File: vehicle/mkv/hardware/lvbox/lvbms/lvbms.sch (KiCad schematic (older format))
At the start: 135 parts, among them J1 CONN_02X03, J2 NanoFit_RA_SMT_04, J3 NanoFit_RA_SMT_02, J4 NanoFit_RA_SMT_02, J5 NanoFit_RA_SMT_02, J6 NanoFit_RA_SMT_02, J7 NanoFit_RA_SMT_02, J8 NanoFit_RA_SMT_06_A, J9 NanoFit_RA_SMT_02, Q1 NSS1C201MZ4, Q2 SQM110P06, Q3 SSM3K333R, Q4 SSM3K333R, Q5 SQM110P06, Q6 BSS138, Q7 SQM110P06, Q8 SQM110P06, U1 MCP2561-E_SN, U10 ACHS-7124, U11 redcube-7461057, U2 ATMEGA16M1, U3 LTC6810HG-2, U4 LT3066IMSE-5, U5 LT1017IS8, U9 redcube-7461057, Y1 Crystal_SMD

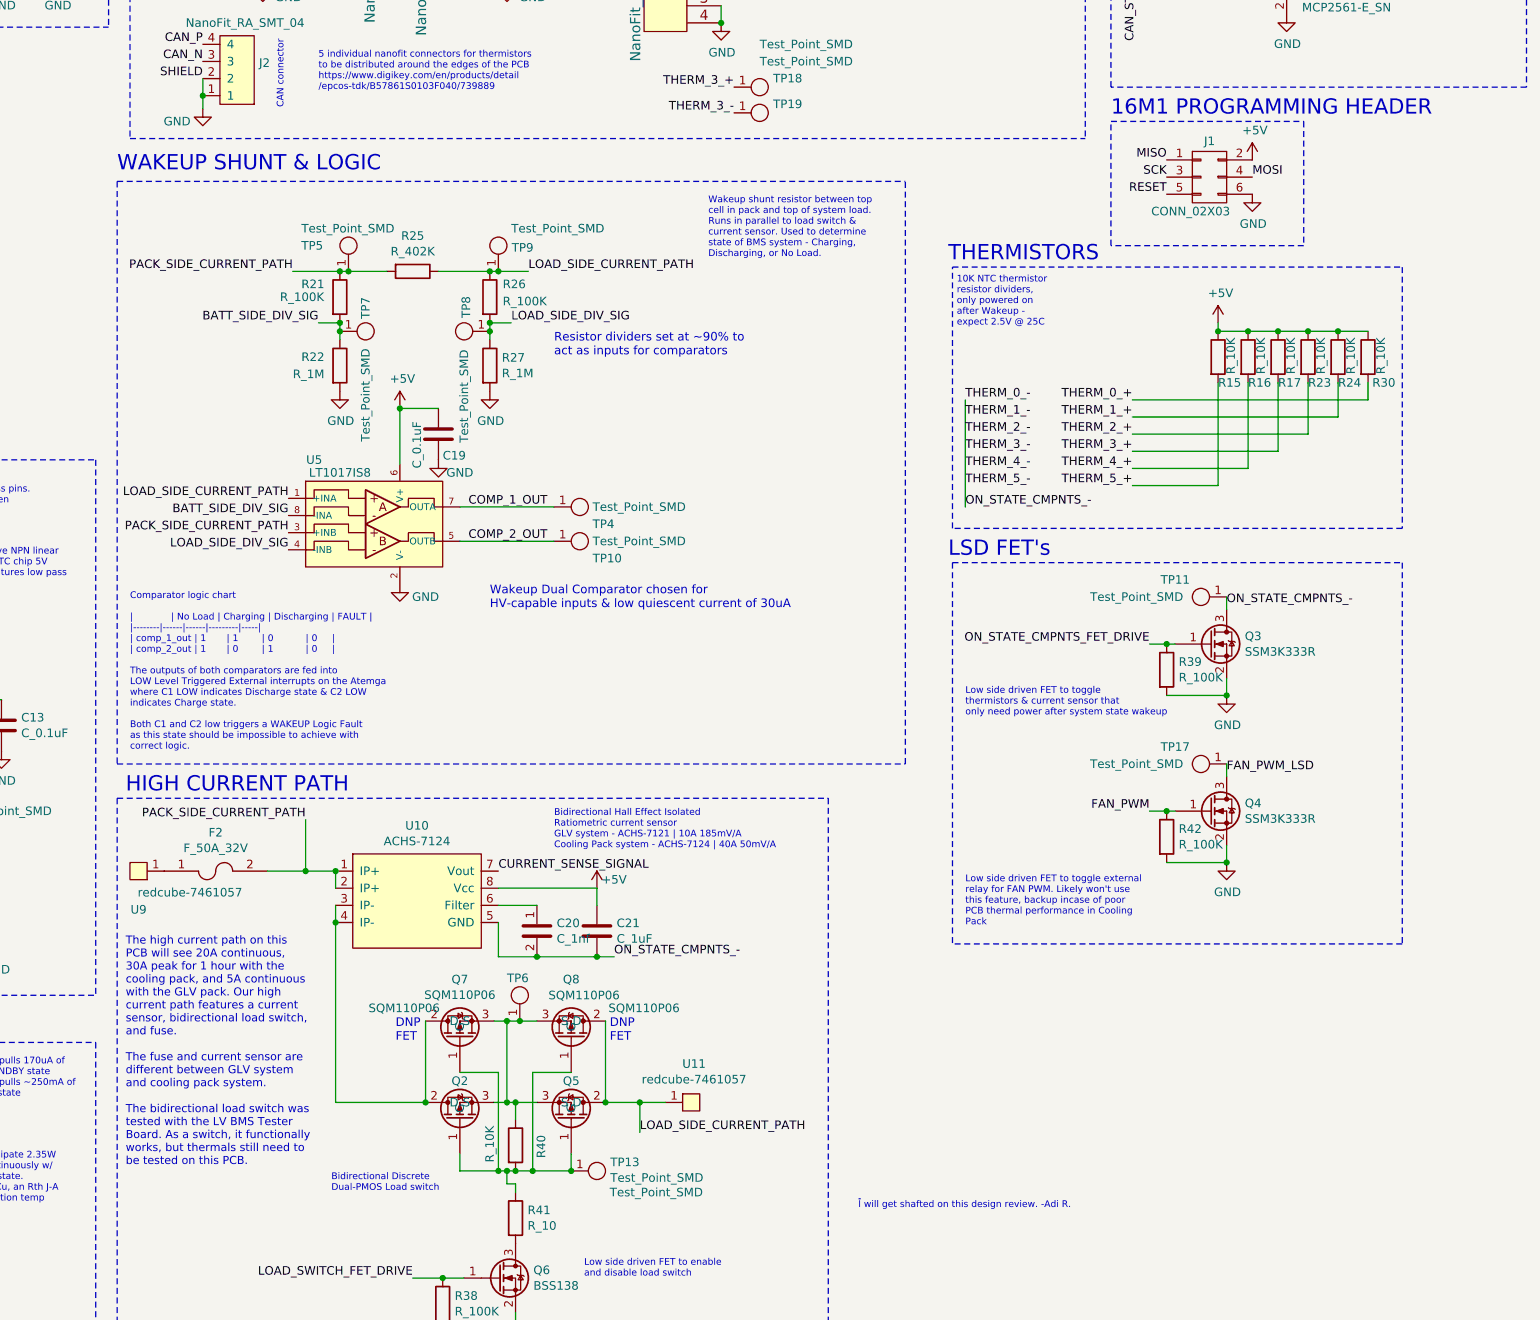
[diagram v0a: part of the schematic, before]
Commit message: updated SPI lib for peripheral A, testing LVBMS SPI, spi_write_read inside ltc681x.c read68 cmd blocks superloop
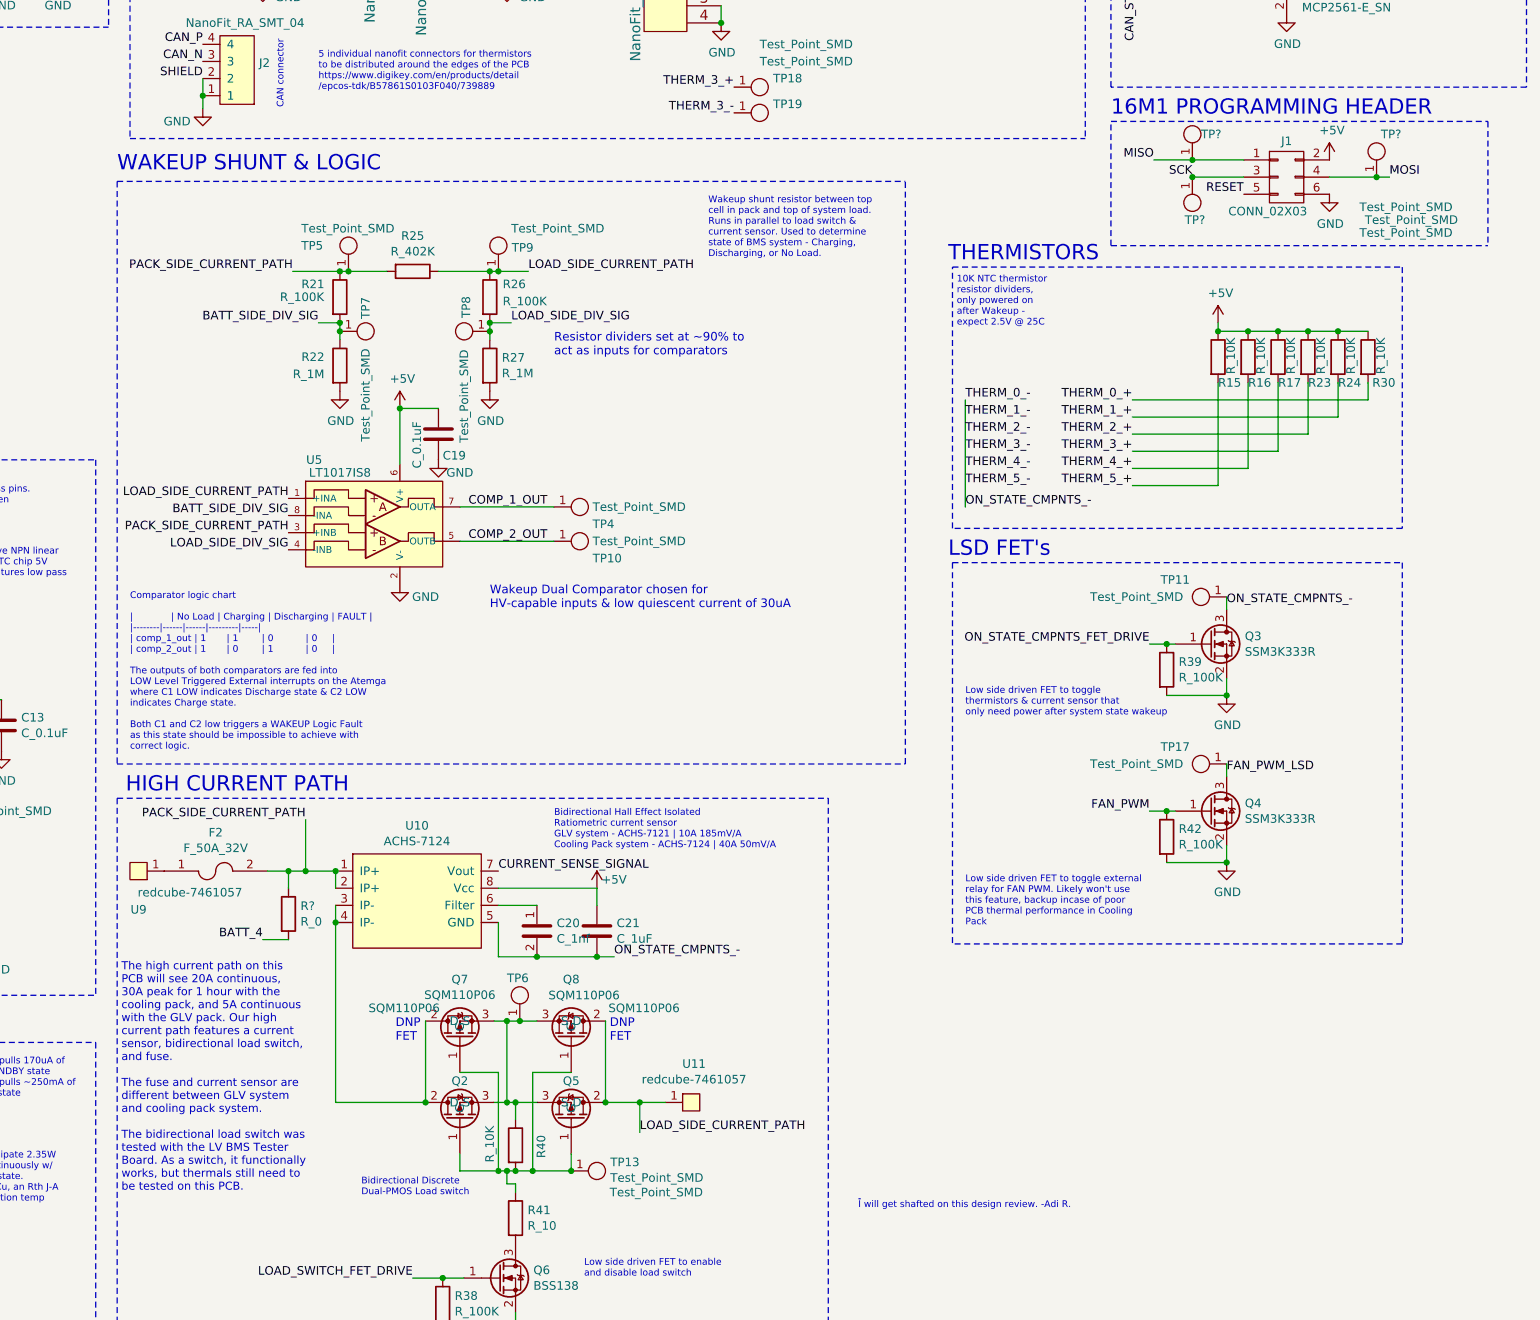
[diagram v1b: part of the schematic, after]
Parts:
- added R?: R_0, footprints:R_0603_1608Metric, symbol formula:R_0
- added TP? (x3): Test_Point_SMD, TestPoint:TestPoint_Pad_D1.5mm, symbol formula:Test_Point_SMD
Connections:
- net BATT_4: now also R?.2
- net MISO: now also TP?.1
- net MOSI: now also TP?.1
- net PACK_SIDE_CURRENT_PATH: now also R?.1
- net SCK: now also TP?.1
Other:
- moved on the sheet: J1
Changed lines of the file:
@@
 L formula:CONN_02X03 J1
 U 1 1 5D628C9D
-P 14350 3400
-F 0 "J1" H 14350 3610 50  0000 C CNN
-F 1 "CONN_02X03" H 14240 3200 50  0000 C CNN
-F 2 "footprints:Pin_Header_Straight_2x03" H 14350 2200 50  0001 C CNN
-F 3 "http://portal.fciconnect.com/Comergent//fci/drawing/67996.pdf" H 14350 2200 50  0001 C CNN
-F 4 "DK" H 14350 3400 60  0001 C CNN "MFN"
-F 5 "609-3234-ND" H 14350 3400 60  0001 C CNN "MPN"
-F 6 "https://www.digikey.com/product-detail/en/amphenol-fci/67997-206HLF/609-3234-ND/1878491" H 14750 4000 60  0001 C CNN "PurchasingLink"
-	1    14350 3400
+P 14800 3400
+F 0 "J1" H 14800 3610 50  0000 C CNN
+F 1 "CONN_02X03" H 14690 3200 50  0000 C CNN
+F 2 "footprints:Pin_Header_Straight_2x03" H 14800 2200 50  0001 C CNN
+F 3 "http://portal.fciconnect.com/Comergent//fci/drawing/67996.pdf" H 14800 2200 50  0001 C CNN
+F 4 "DK" H 14800 3400 60  0001 C CNN "MFN"
+F 5 "609-3234-ND" H 14800 3400 60  0001 C CNN "MPN"
+F 6 "https://www.digikey.com/product-detail/en/amphenol-fci/67997-206HLF/609-3234-ND/1878491" H 15200 4000 60  0001 C CNN "PurchasingLink"
+	1    14800 3400
 	1    0    0    -1
 $EndComp
-Text Label 14100 3300 2    50   ~ 0
+Text Label 14025 3300 2    50   ~ 0
 MISO
-Text Label 14100 3400 2    50   ~ 0
+Text Label 14250 3400 2    50   ~ 0
 SCK
-Text Label 14100 3500 2    50   ~ 0
+Text Label 14550 3500 2    50   ~ 0
 RESET
-Text Label 14600 3400 0    50   ~ 0
+Text Label 15400 3400 0    50   ~ 0
 MOSI
 Text Notes 13775 3050 0    89   ~ 0
@@
 	550  4775 550  550
 Wire Notes Line
-	13775 3075 14900 3075
-Wire Notes Line
-	14900 3075 14900 3800
-Wire Notes Line
-	14900 3800 13775 3800
-Wire Notes Line
 	13775 3800 13775 3075
 Wire Notes Line
@@
 PACK_SIDE_CURRENT_PATH
 Wire Wire Line
-	8850 7450 9075 7450
+	8850 7450 8975 7450
 Connection ~ 9075 7450
 Wire Wire Line
@@
 Text Notes 8025 7000 0    89   ~ 0
 HIGH CURRENT PATH\n
-Text Notes 9225 9325 0    39   ~ 0
+Text Notes 9400 9350 0    39   ~ 0
 Bidirectional Discrete \nDual-PMOS Load switch
 $Comp
@@
 L power:+5V #PWR?
 U 1 1 61977052
-P 14600 3300
-F 0 "#PWR?" H 14600 3150 50  0001 C CNN
-F 1 "+5V" H 14615 3473 50  0000 C CNN
-F 2 "" H 14600 3300 50  0001 C CNN
-F 3 "" H 14600 3300 50  0001 C CNN
-	1    14600 3300
+P 15050 3300
+F 0 "#PWR?" H 15050 3150 50  0001 C CNN
+F 1 "+5V" H 15065 3473 50  0000 C CNN
+F 2 "" H 15050 3300 50  0001 C CNN
+F 3 "" H 15050 3300 50  0001 C CNN
+	1    15050 3300
 	1    0    0    -1
 $EndComp
@@
 L power:GND #PWR?
 U 1 1 61BB84B2
-P 14600 3500
-F 0 "#PWR?" H 14600 3250 50  0001 C CNN
-F 1 "GND" H 14605 3327 50  0000 C CNN
-F 2 "" H 14600 3500 50  0001 C CNN
-F 3 "" H 14600 3500 50  0001 C CNN
-	1    14600 3500
+P 15050 3500
+F 0 "#PWR?" H 15050 3250 50  0001 C CNN
+F 1 "GND" H 15055 3327 50  0000 C CNN
+F 2 "" H 15050 3500 50  0001 C CNN
+F 3 "" H 15050 3500 50  0001 C CNN
+	1    15050 3500
 	1    0    0    -1
 $EndComp
@@
 	1    0    0    -1
 $EndComp
-Text Notes 8025 9175 0    47   ~ 0
+Text Notes 8000 9325 0    47   ~ 0
 The high current path on this \nPCB will see 20A continuous, \n30A peak for 1 hour with the \ncooling pack, and 5A continuous \nwith the GLV pack. Our high \ncurrent path features a current \nsensor, bidirectional load switch, \nand fuse.  \n\nThe fuse and current sensor are \ndifferent between GLV system \nand cooling pack system. \n\nThe bidirectional load switch was \ntested with the LV BMS Tester \nBoard. As a switch, it functionally \nworks, but thermals still need to \nbe tested on this PCB.
 Wire Notes Line
@@
 Wire Notes Line
 	8050 3175 13625 3175
+Wire Wire Line
+	8975 7450 8975 7550
+Connection ~ 8975 7450
+Wire Wire Line
+	8975 7450 9075 7450
+$Comp
+L formula:R_0 R?
+U 1 1 62672ADF
+P 8975 7700
+F 0 "R?" H 9045 7746 50  0000 L CNN
+F 1 "R_0" H 9045 7655 50  0000 L CNN
+F 2 "footprints:R_0603_1608Metric" H 8905 7700 50  0001 C CNN
+F 3 "http://industrial.panasonic.com/www-cgi/jvcr13pz.cgi?E+PZ+3+AOA0001+ERJ3GEY0R00V+7+WW" H 9055 7700 50  0001 C CNN
+F 4 "DK" H 8975 7700 60  0001 C CNN "MFN"
+F 5 "P0.0GCT-ND" H 8975 7700 60  0001 C CNN "MPN"
+F 6 "https://www.digikey.com/product-detail/en/panasonic-electronic-components/ERJ-3GEY0R00V/P0.0GCT-ND/134711" H 9455 8100 60  0001 C CNN "PurchasingLink"
+	1    8975 7700
+	1    0    0    -1
+$EndComp
+Text Label 8825 7850 2    50   ~ 0
+BATT_4
+Wire Wire Line
+	8825 7850 8975 7850
+Wire Wire Line
+	15050 3400 15325 3400
+Wire Wire Line
+	14550 3400 14250 3400
+Wire Wire Line
+	14025 3300 14250 3300
+$Comp
+L formula:Test_Point_SMD TP?
+U 1 1 62705BA6
+P 14250 3250
+F 0 "TP?" H 14300 3350 50  0000 L CNN
+F 1 "Test_Point_SMD" H 15225 2775 50  0000 L CNN
+F 2 "TestPoint:TestPoint_Pad_D1.5mm" H 14250 3100 50  0001 C CNN
+F 3 "" H 14250 3250 50  0001 C CNN
+	1    14250 3250
+	1    0    0    -1
+$EndComp
+$Comp
+L formula:Test_Point_SMD TP?
+U 1 1 6271D460
+P 14250 3450
+F 0 "TP?" H 14175 3650 50  0000 L CNN
+F 1 "Test_Point_SMD" H 12700 3650 50  0000 L CNN
+F 2 "TestPoint:TestPoint_Pad_D1.5mm" H 14250 3300 50  0001 C CNN
+F 3 "" H 14250 3450 50  0001 C CNN
+	1    14250 3450
+	-1   0    0    1
+$EndComp
+$Comp
+L formula:Test_Point_SMD TP?
+U 1 1 62734A65
+P 15325 3350
+F 0 "TP?" H 15350 3550 50  0000 L CNN
+F 1 "Test_Point_SMD" H 15225 3125 50  0000 L CNN
+F 2 "TestPoint:TestPoint_Pad_D1.5mm" H 15325 3200 50  0001 C CNN
+F 3 "" H 15325 3350 50  0001 C CNN
+	1    15325 3350
+	1    0    0    -1
+$EndComp
+Wire Notes Line
+	15975 3075 15975 3800
+Wire Notes Line
+	13775 3075 15975 3075
+Wire Notes Line
+	13775 3800 15975 3800
+Connection ~ 15325 3400
+Wire Wire Line
+	15325 3400 15400 3400
+Connection ~ 14250 3300
+Wire Wire Line
+	14250 3300 14550 3300
+Connection ~ 14250 3400
 $EndSCHEMATC

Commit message: minor hardware updates, working on comparator wakeup circuitry
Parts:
- added Q10, Q9: SSM3K333R, footprints:SOT-23F, symbol formula:SSM3K333R
- added R31, R48, R49: R_10K, footprints:R_0805_OEM, symbol formula:R_10K
- added S1: Switch_NO, SW_TL3315NF100Q, symbol formula:Switch_NO
- added TP29, TP30: Test_Point_SMD, TestPoint:TestPoint_Pad_D1.5mm, symbol formula:Test_Point_SMD
- gave numbers to parts that had none: 4
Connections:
- net +5V: now also R48.1, R49.1, S1.1, S1.2; no longer C19.1, U5.6 (V+)
- net BATT_4: now also C19.1, U5.6 (V+)
- net BATT_SIDE_DIV_SIG: now also U5.1 (+INA); no longer U5.8 (-INA)
- net COMP_1_OUT: no longer TP4.1, U5.7 (OUTA)
- net COMP_2_OUT: no longer TP10.1, U5.5 (OUTB)
- net GND: now also Q10.2 (S), Q9.2 (S), R31.2
- net LOAD_SIDE_CURRENT_PATH: now also U5.8 (-INA); no longer U5.1 (+INA)
- net LOAD_SIDE_DIV_SIG: now also U5.3 (+INB); no longer U5.4 (-INB)
- net ON_STATE_CMPNTS_FET_DRIVE: now also U2.29 ((PCINT16/PSCOUT0A)PD0); no longer U2.30 ((PCINT8/INT3/PSCOUT1A)PC0)
- net PACK_SIDE_CURRENT_PATH: now also U5.4 (-INB); no longer U5.3 (+INB)
- new net: Q9.1 (G), TP4.1, U5.7 (OUTA)
- new net: Q10.1 (G), TP10.1, U5.5 (OUTB)
- new net BTN: R31.1, S1.3, S1.4, U2.30 ((PCINT8/INT3/PSCOUT1A)PC0)
- new net COMP_1_SIG: Q9.3 (D), R48.2, TP29.1
- new net COMP_2_SIG: Q10.3 (D), R49.2, TP30.1
- no-connect marks 14 -> 13
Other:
- note added: "Comparator logic chart \n\n| | No Load | Charging | Discharging | FAULT |\n|--------|------|------|---------|-----|\n| comp_1_sig | 1 | 1 | 0 | 0 |\n| comp_2_sig | 1 | 0 | 1 | 0 |\n\nThe outputs of both comparators are fed into \nLOW Level Triggered External interrupts on the Atemga\nwhere C1 LOW indicates Discharge state & C2 LOW \nindicates Charge state. \n\nBoth C1 and C2 low triggers a WAKEUP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"
- note added: "LEDS & Button"
- note added: "Manual Reset Button on \nexternal interrupt / GPIO \nin case wakeup circuitry \ndoesn't work"
- note removed: "Comparator logic chart \n\n| | No Load | Charging | Discharging | FAULT |\n|--------|------|------|---------|-----|\n| comp_1_out | 1 | 1 | 0 | 0 |\n| comp_2_out | 1 | 0 | 1 | 0 |\n\nThe outputs of both comparators are fed into \nLOW Level Triggered External interrupts on the Atemga\nwhere C1 LOW indicates Discharge state & C2 LOW \nindicates Charge state. \n\nBoth C1 and C2 low triggers a WAKEUP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"
- note removed: "LEDS"
- moved on the sheet: D1, D2, D3, D4, D5, Q3, Q4, R32, R34, R35, R36, R39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
